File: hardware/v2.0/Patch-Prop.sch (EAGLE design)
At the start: 49 parts, among them IC1 TPS77033, IC2 ATMEGA168, IC3 MCP1253, IC5 MMA8452Q, IC6 W2RV005RM, IC7 MCP73831

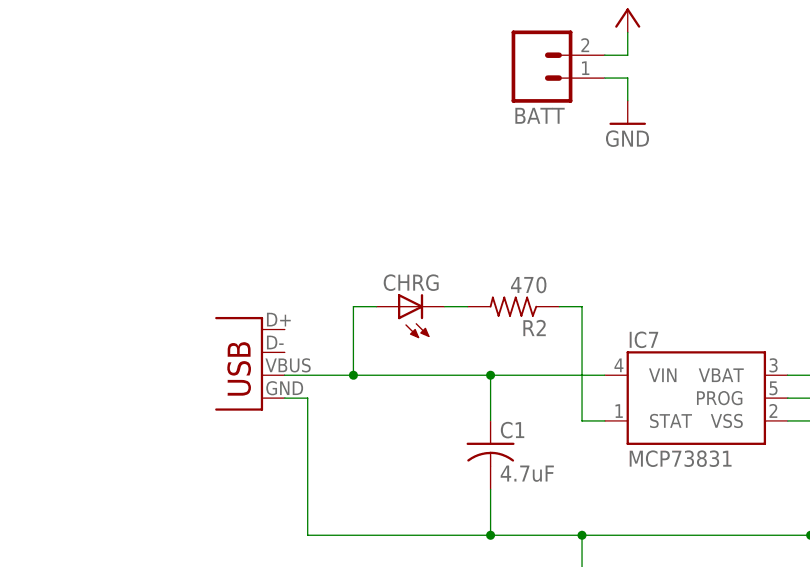
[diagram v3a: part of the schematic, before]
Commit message: Some small fixes, bigger font. First pass gerber file
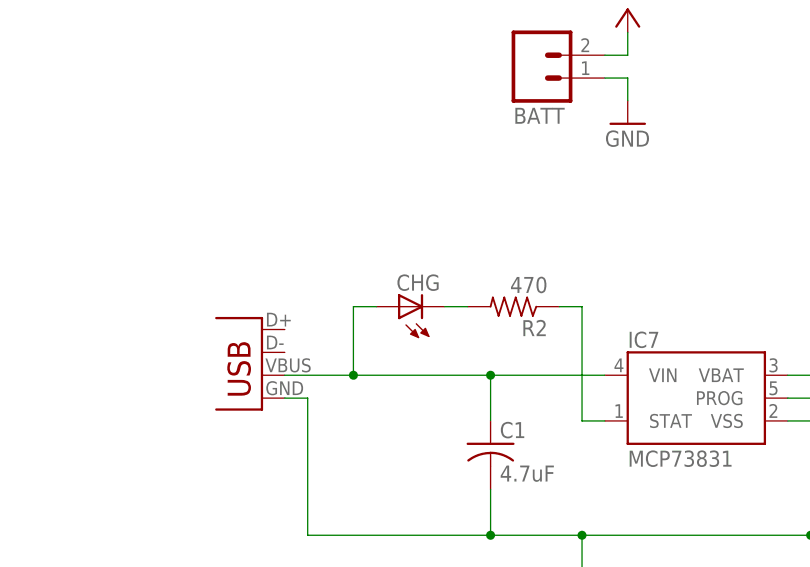
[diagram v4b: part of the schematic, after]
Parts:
- renumbered CHRG to CHG
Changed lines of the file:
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@@
 <part name="SUPPLY7" library="supply2" deviceset="V+" device=""/>
 <part name="SUPPLY8" library="supply2" deviceset="V+" device=""/>
-<part name="CHRG" library="led" deviceset="LED" device="CHIPLED_0805"/>
+<part name="CHG" library="led" deviceset="LED" device="CHIPLED_0805"/>
 <part name="R2" library="rcl" deviceset="R-US_" device="R0603" value="470"/>
 <part name="R3" library="rcl" deviceset="R-US_" device="R0603" value="2k"/>
@@
 <instance part="SUPPLY7" gate="1" x="401.32" y="129.54"/>
 <instance part="SUPPLY8" gate="1" x="515.62" y="106.68"/>
-<instance part="CHRG" gate="G$1" x="81.28" y="345.44" rot="R90"/>
+<instance part="CHG" gate="G$1" x="81.28" y="345.44" rot="R90"/>
 <instance part="R2" gate="G$1" x="93.98" y="345.44" rot="R180"/>
 <instance part="R3" gate="G$1" x="132.08" y="327.66" rot="R270"/>
@@
 <pinref part="IC7" gate="G$1" pin="VIN"/>
 <pinref part="C1" gate="G$1" pin="1"/>
-<pinref part="CHRG" gate="G$1" pin="A"/>
+<pinref part="CHG" gate="G$1" pin="A"/>
 <wire x1="78.74" y1="345.44" x2="76.2" y2="345.44" width="0.1524" layer="91"/>
 <wire x1="76.2" y1="345.44" x2="76.2" y2="337.82" width="0.1524" layer="91"/>
@@
 <segment>
 <wire x1="88.9" y1="345.44" x2="86.36" y2="345.44" width="0.1524" layer="91"/>
-<pinref part="CHRG" gate="G$1" pin="C"/>
+<pinref part="CHG" gate="G$1" pin="C"/>
 <pinref part="R2" gate="G$1" pin="2"/>
 </segment>
